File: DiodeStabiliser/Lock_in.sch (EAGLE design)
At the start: 53 parts, among them IC2 AD712N, IC3 AD712N, IC4 74AC04N

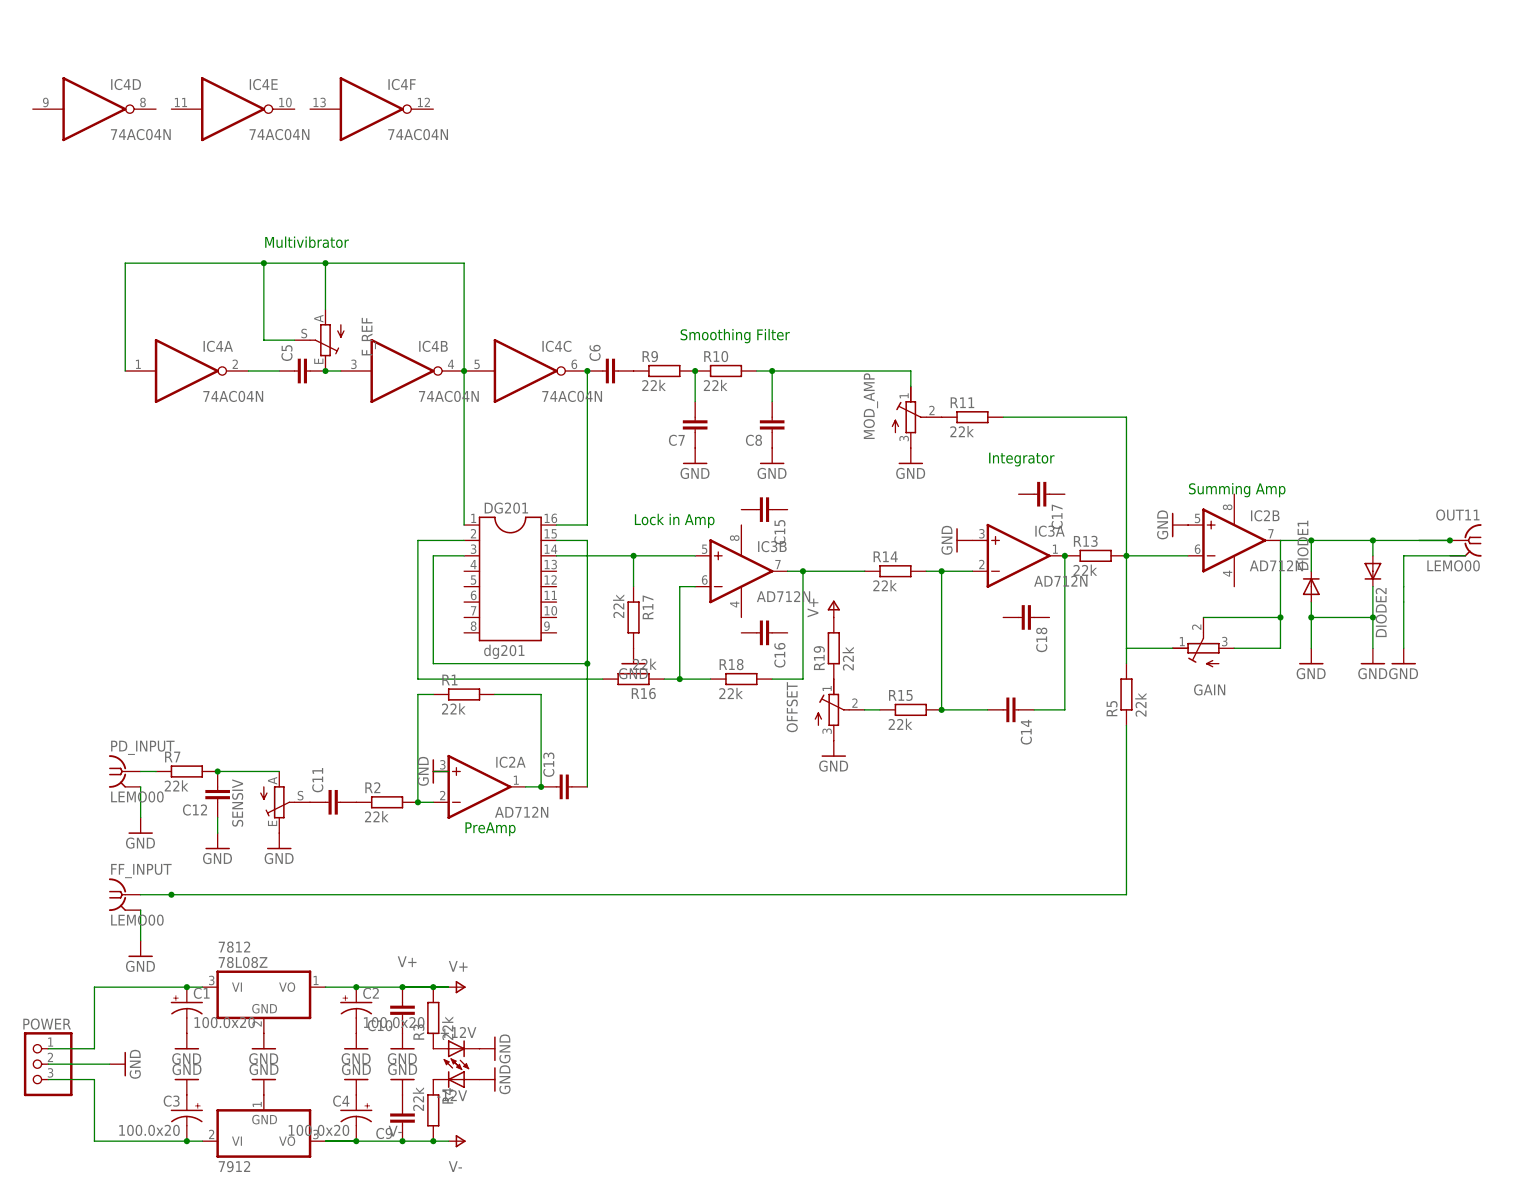
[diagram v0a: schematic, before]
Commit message: New version of the diode stabliser circuit
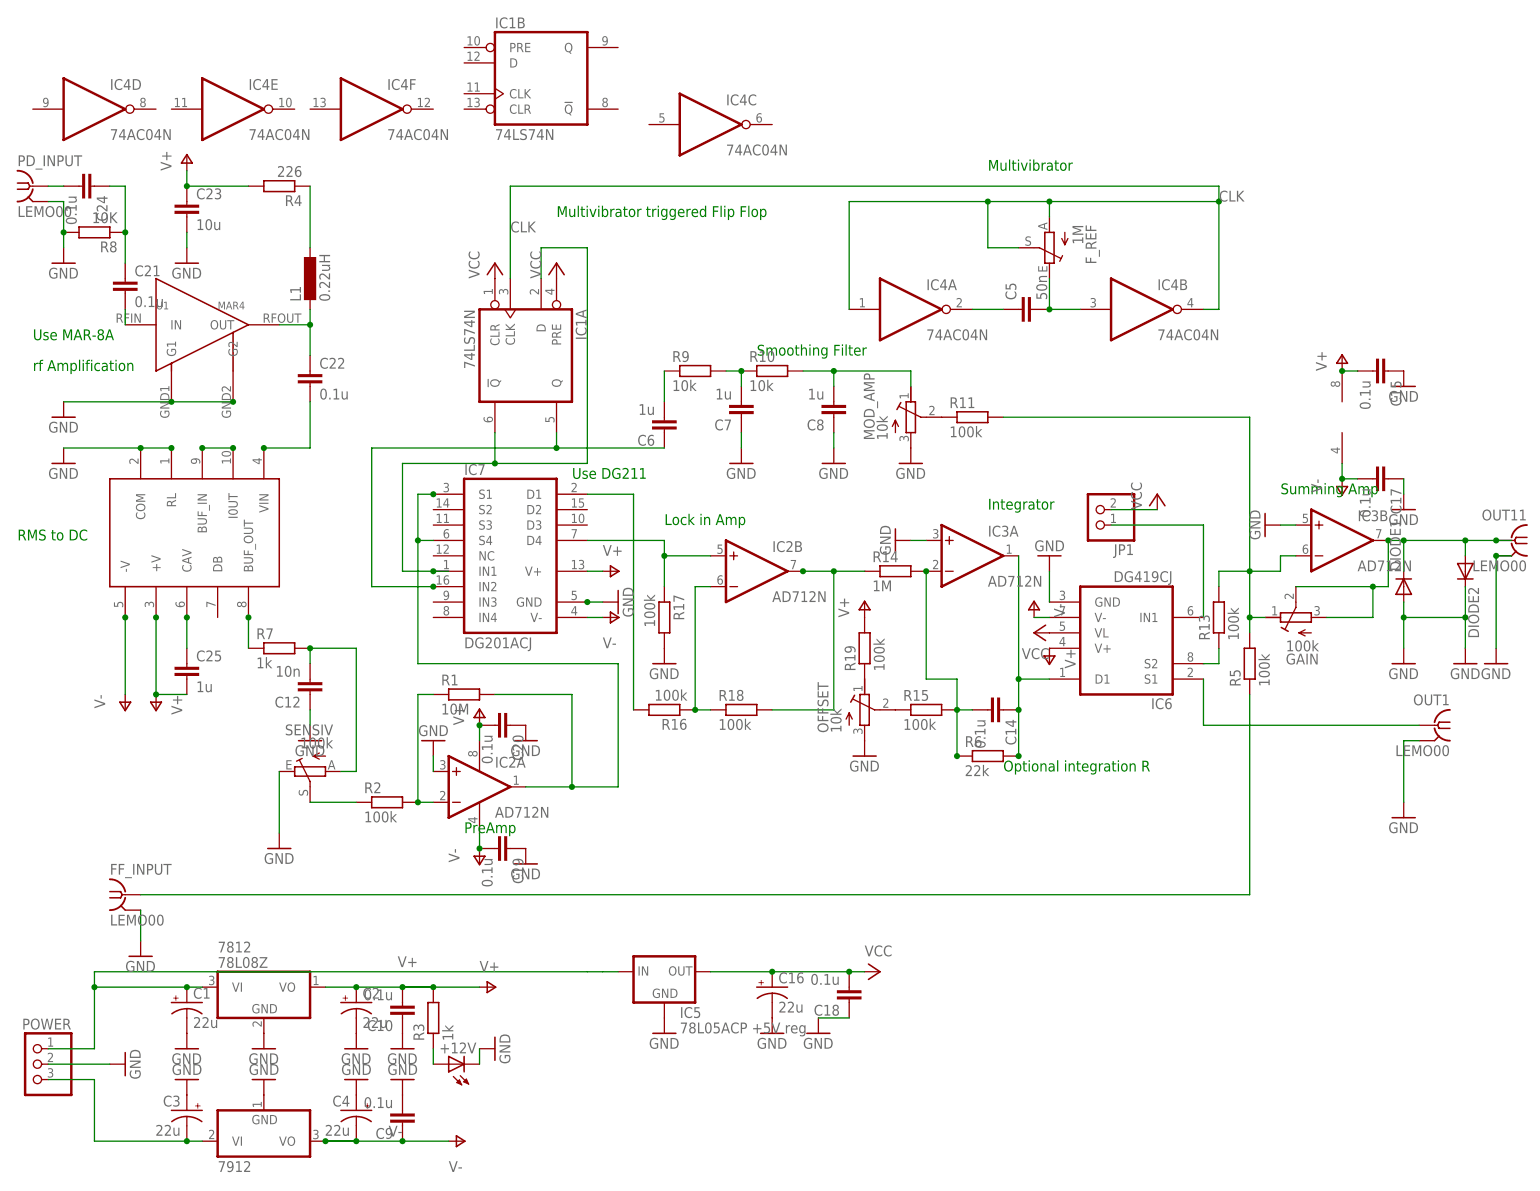
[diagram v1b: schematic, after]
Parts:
- removed -12V: (no value), led:LED5MM
- removed C11, C13: (no value), rcl:C-EU050-024X044
- removed DG201: dg201, ic-package:DIL16
- added C19, C20: 0.1u, rcl:C-EU050-024X044
- added C21, C22, C24: 0.1u, rcl:C-EUC0805
- added C23: 10u, rcl:C-EUC1206
- added C25: 1u, rcl:C-EUC0805
- added IC1: 74LS74N, 74xx-eu:74LS74N
- added IC5: 78L05ACP +5V reg, v-reg:78LXX
- added IC6: DG419CJ, maxim:DG419CJ
- added IC7: DG201ACJ, maxim:DG201ACJ
- added JP1: (no value), pinhead:PINHD-1X2
- added L1: 0.22uH, rcl:L-EUL3216C
- added OUT1: LEMO00, con-coax:LEMO00
- added R6: 22k, rcl:R-EU_0204/7
- added R8: 10K, rcl:R-EU_R1206
- added U$1: AD636, analog-devices:AD636
- added U1: MAR4, custom_parts:MAR4
- C1, C2, C3, C4: value 100.0x20 -> 22u
- C10, C14, C15, C17, C18, C9: value (none) -> 0.1u
- C12: value (none) -> 10n
- C16: value (none) -> 22u; device rcl:C-EU050-024X044 -> rcl:CPOL-USE5-4
- C5: value (none) -> 50n
- C6, C7, C8: value (none) -> 1u
- F_REF: value (none) -> 1M; device pot:TRIM_EU-CA9V -> pot:TRIM_EU-S63P
- GAIN: value (none) -> 100k
- MOD_AMP, OFFSET: value (none) -> 10k
- R1: value 22k -> 10M
- R10, R9: value 22k -> 10k
- R11, R13, R15, R16, R17, R18, R19, R2, R5: value 22k -> 100k
- R14: value 22k -> 1M
- R3, R7: value 22k -> 1k
- R4: value 22k -> 226; device rcl:R-EU_0204/7 -> rcl:R-EU_R1206
- SENSIV: value (none) -> 100k; device pot:TRIM_EU-CA9V -> pot:TRIM_EU-S63P
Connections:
- removed net F1: DG201.1, F_REF.A, F_REF.S, IC4A.I, IC4B.O, IC4C.I
- removed net N$17: DIODE1.C, DIODE2.A, GAIN.E, GAIN.S, IC2B.OUT, OUT11.1
- removed net N$7: C11.2, R2.1
- removed net N$8: C11.1, SENSIV.S
- new net CLK: F_REF.A, F_REF.S, IC1A.CLK, IC4A.I, IC4B.O
- new net GND1: IC6.IN1, JP1.1
- new net N$19: IC6.S2, R13.1
- new net N$27: C21.2, U1.IN
- new net N$28: C14.1, IC3A.OUT, IC6.D1, R6.2
- new net N$29: L1.1, R4.1
- new net N$30: C22.1, L1.2, U1.OUT
- new net N$32: C24.2, PD_INPUT.1
- new net N$33: C21.1, C24.1, R8.1
- new net N$34: C22.2, U$1.VIN
- new net N$35: IC6.S1, OUT1.1
- new net N$37: U$1.BUF_IN, U$1.I0UT
- new net N$38: C25.1, U$1.CAV
- new net VCC: C16.+, C18.2, IC1A.CLR, IC1A.PRE, IC5.OUT, IC6.VL, JP1.2
- net F2: now also IC1A.Q, IC7.IN2; no longer DG201.16, IC4C.O
- net GND: now also C15.1, C16.-, C17.1, C18.1, C19.1, C20.1, C23.2, IC3B.+IN, IC5.GND, IC6.GND, IC7.GND, OUT1.GND, OUT11.GND, R8.2, U$1.COM, U$1.RL, U1.G1, U1.G2; no longer -12V.A, IC2B.+IN
- net N$10: now also U$1.BUF_OUT; no longer PD_INPUT.1
- net N$14: now also IC3B.-IN; no longer IC2B.-IN
- net N$16: now also IC2A.OUT, IC7.S1, IC7.S4, R1.2; no longer C13.2, DG201.15, DG201.3
- net N$20: now also IC1A.!Q, IC1A.D, IC7.IN1; no longer C14.1, IC3A.OUT, R13.1
- net N$21: now also R6.1
- net N$22: now also IC7.D1; no longer DG201.2
- net N$23: now also IC2B.+IN, IC7.D4; no longer DG201.14, IC3B.+IN
- net N$24: now also IC2B.-IN; no longer IC3B.-IN
- net N$25: now also IC2B.OUT; no longer IC3B.OUT
- net N$3: now also DIODE1.C, DIODE2.A, GAIN.E, GAIN.S, IC3B.OUT, OUT11.1; no longer -12V.C, R4.1
- net N$6: now also R2.1, SENSIV.S; no longer C13.1, IC2A.OUT, R1.2
- net V+: now also C15.2, C20.2, C23.1, C25.2, IC2P.V+, IC3P.V+, IC6.V+, IC7.V+, R4.2, U$1.+V
- net V+INPUT: now also IC5.IN
- net V-: now also C17.2, C19.2, IC2P.V-, IC3P.V-, IC6.V-, IC7.V-, U$1.-V; no longer R4.2
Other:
- note added: "Multivibrator triggered Flip Flop"
- note added: "Optional integration R"
- note added: "RMS to DC"
- note added: "Use DG211"
- note added: "Use MAR-8A"
- note added: "rf Amplification"
- moved on the sheet: +12V, C12, C14, C15, C17, C18, C5, C6, C7, C8, DIODE1, DIODE2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
